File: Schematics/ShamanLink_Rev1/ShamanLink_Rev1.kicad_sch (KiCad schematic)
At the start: 37 parts, among them J6 USB4105-GF-A, U1 LPC55S69JBD64K

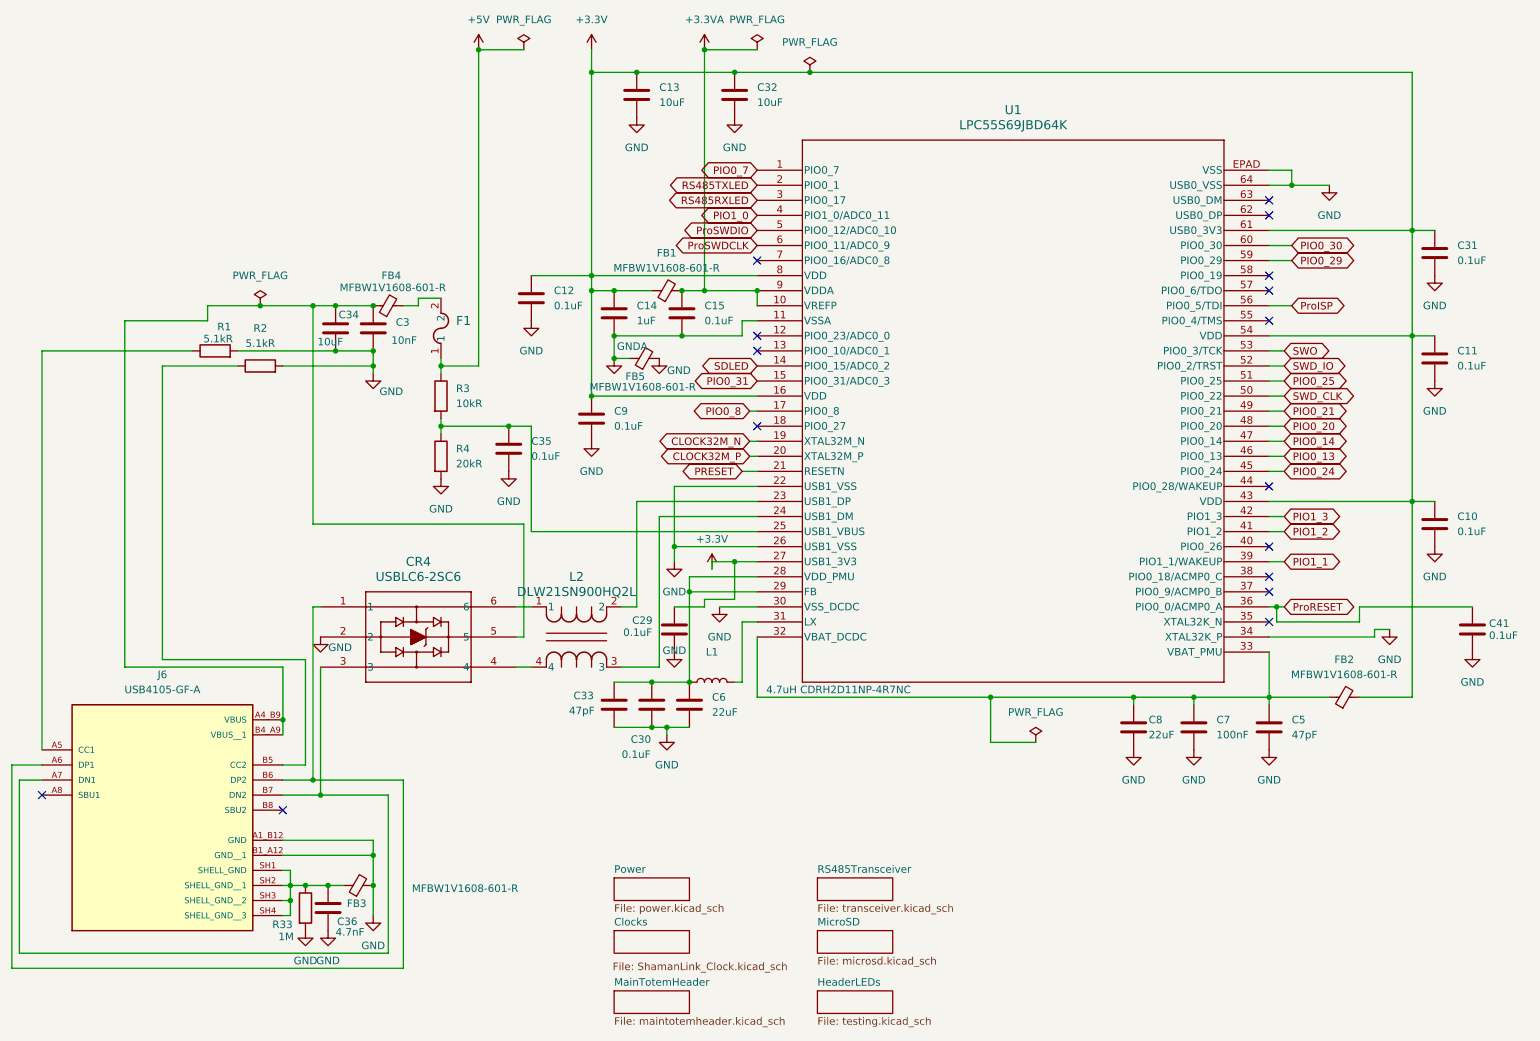
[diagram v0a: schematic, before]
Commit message: Final ShamanLink Revisions and Motor Totem Final Revisions
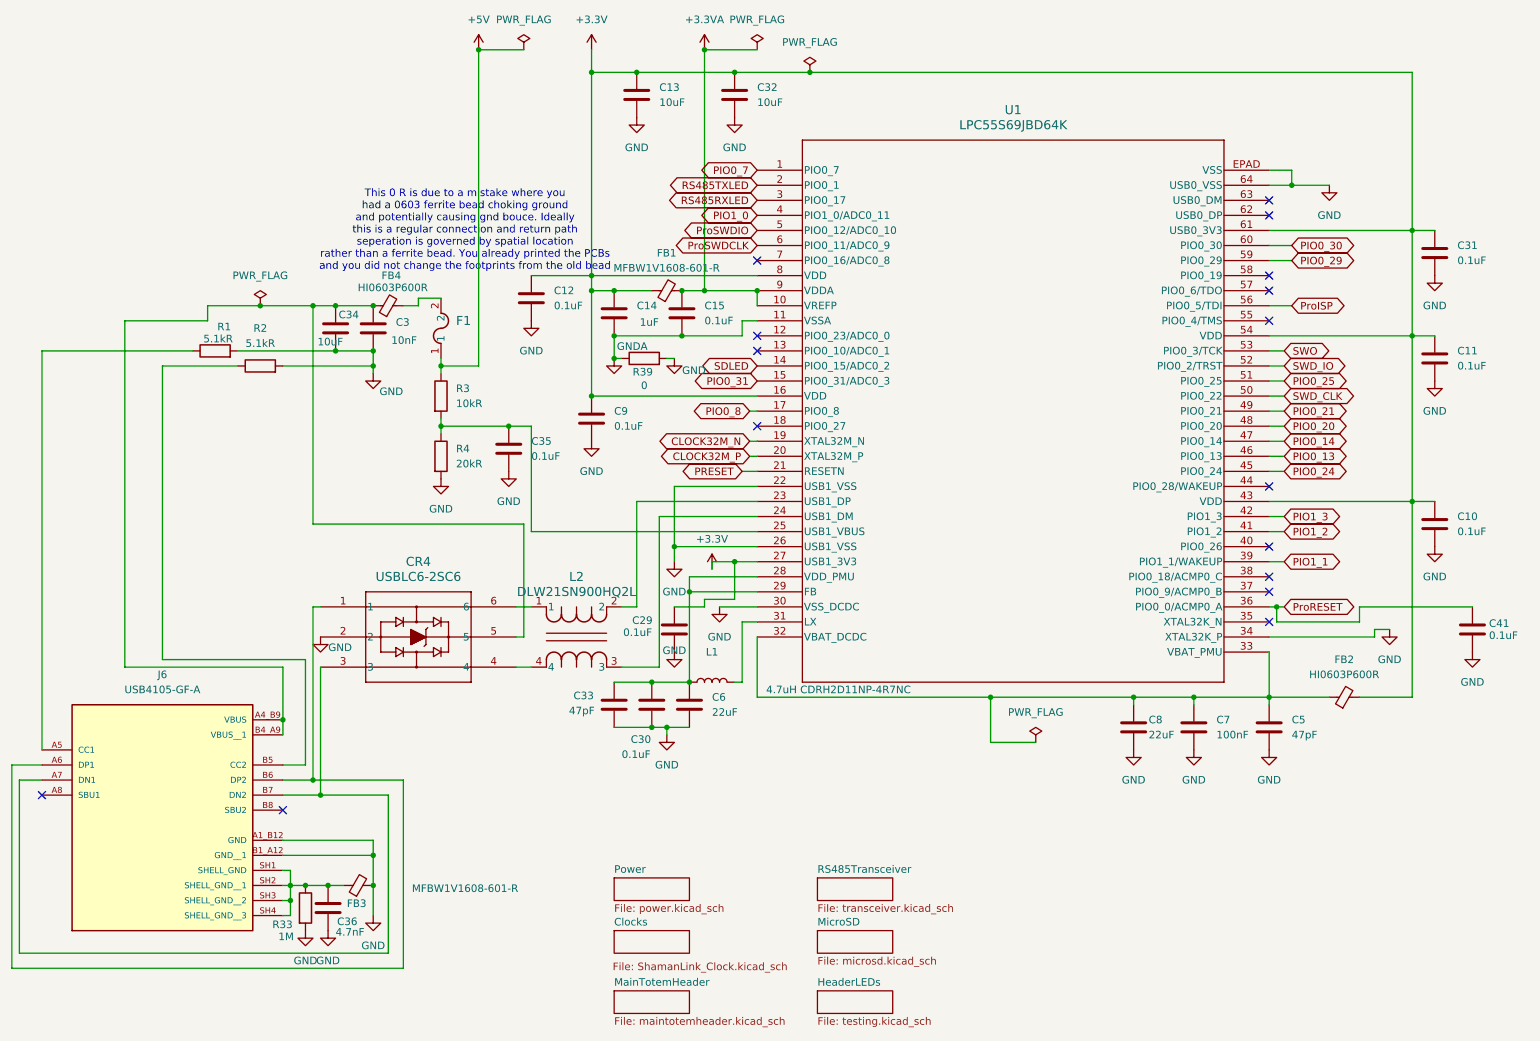
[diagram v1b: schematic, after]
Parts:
- removed FB5: MFBW1V1608-601-R, Resistor_SMD:R_0603_1608Metric_Pad0.98x0.95mm_HandSolder, symbol Device:FerriteBead_Small
- added R39: 0, symbol Device:R
- FB2, FB4: value MFBW1V1608-601-R -> HI0603P600R
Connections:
- net GND: now also R39.2
- net GNDA: now also R39.1
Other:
- note added: "This 0 R is due to a mistake where you had a 0603 ferrite bead choking ground and potentially causing gnd bouce. Ideally this is a regular connection and return path seperation is governed by spatial location rather than a ferrite bead. You already printed the PCBs and you did not change the footprints from the old bead"
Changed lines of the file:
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@@
 		(title "MCU and USB")
 	)
+	(text "This 0 R is due to a mistake where you \nhad a 0603 ferrite bead choking ground\nand potentially causing gnd bouce. Ideally\nthis is a regular connection and return path \nseperation is governed by spatial location \nrather than a ferrite bead. You already printed the PCBs\nand you did not change the footprints from the old bead"
+		(exclude_from_sim no)
+		(at 90.424 63.5 0)
+		(effects
+			(font
+				(size 1.27 1.27)
+			)
+		)
+	)
 	(junction
 		(at 115.57 73.66)
@@
 	)
 	(junction
-		(at 68.58 83.82)
+		(at 115.57 85.09)
 		(diameter 0)
 		(color 0 0 0 0)
 	)
 	(junction
-		(at 60.96 176.53)
+		(at 68.58 83.82)
 		(diameter 0)
 		(color 0 0 0 0)
 	)
 	(junction
-		(at 111.76 71.12)
+		(at 60.96 176.53)
 		(diameter 0)
 		(color 0 0 0 0)
 	)
 	(junction
-		(at 115.57 85.09)
+		(at 111.76 71.12)
 		(diameter 0)
 		(color 0 0 0 0)
@@
 	(wire
 		(pts
+			(xy 115.57 85.09) (xy 116.84 85.09)
+		)
+		(stroke
+			(width 0)
+			(type default)
+		)
+	)
+	(wire
+		(pts
 			(xy 63.5 135.89) (xy 63.5 153.67)
 		)
@@
 	(wire
 		(pts
+			(xy 124.46 85.09) (xy 125.73 85.09)
+		)
+		(stroke
+			(width 0)
+			(type default)
+		)
+	)
+	(wire
+		(pts
 			(xy 86.36 86.36) (xy 86.36 87.63)
 		)
@@
 	(wire
 		(pts
-			(xy 115.57 85.09) (xy 118.11 85.09)
-		)
-		(stroke
-			(width 0)
-			(type default)
-		)
-	)
-	(wire
-		(pts
 			(xy 74.93 173.99) (xy 74.93 179.07)
 		)
@@
 			)
 		)
-		(property "Value" "MFBW1V1608-601-R"
+		(property "Value" "HI0603P600R"
 			(at 78.232 73.152 90)
 			(effects
@@
 			)
 		)
-		(property "Value" "MFBW1V1608-601-R"
+		(property "Value" "HI0603P600R"
 			(at 238.7219 138.43 90)
 			(effects
@@
 		(on_board yes)
 		(dnp no)
-		(fields_autoplaced yes)
 		(property "Reference" "C14"
 			(at 119.38 76.1999 0)
@@
 		)
 		(property "Value" "1uF"
-			(at 119.38 78.7399 0)
+			(at 119.888 78.994 0)
 			(effects
 				(font
@@
 	(symbol
 		(lib_id "power:GND")
-		(at 123.19 85.09 0)
+		(at 125.73 85.09 0)
 		(unit 1)
 		(exclude_from_sim no)
@@
 		(dnp no)
 		(property "Reference" "#PWR022"
-			(at 123.19 91.44 0)
+			(at 125.73 91.44 0)
 			(effects
 				(font
@@
 		)
 		(property "Value" "GND"
-			(at 126.492 87.122 0)
+			(at 129.032 87.122 0)
 			(effects
 				(font
@@
 		)
 		(property "Footprint" ""
-			(at 123.19 85.09 0)
+			(at 125.73 85.09 0)
 			(effects
 				(font
@@
 		)
 		(property "Datasheet" ""
-			(at 123.19 85.09 0)
+			(at 125.73 85.09 0)
 			(effects
 				(font
@@
 		)
 		(property "Description" "Power symbol creates a global label with name \"GND\" , ground"
-			(at 123.19 85.09 0)
+			(at 125.73 85.09 0)
 			(effects
 				(font
@@
 	)
 	(symbol
+		(lib_id "Device:R")
+		(at 120.65 85.09 90)
+		(unit 1)
+		(exclude_from_sim no)
+		(in_bom yes)
+		(on_board yes)
+		(dnp no)
+		(property "Reference" "R39"
+			(at 120.396 87.376 90)
+			(effects
+				(font
+					(size 1.27 1.27)
+				)
+			)
+		)
+		(property "Value" "0"
+			(at 120.65 89.662 90)
+			(effects
+				(font
+					(size 1.27 1.27)
+				)
+			)
+		)
+		(property "Footprint" ""
+			(at 120.65 86.868 90)
+			(effects
+				(font
+					(size 1.27 1.27)
+				)
+				(hide yes)
+			)
+		)
+		(property "Datasheet" "~"
+			(at 120.65 85.09 0)
+			(effects
+				(font
+					(size 1.27 1.27)
+				)
+				(hide yes)
+			)
+		)
+		(property "Description" "Resistor"
+			(at 120.65 85.09 0)
+			(effects
+				(font
+					(size 1.27 1.27)
+				)
+				(hide yes)
+			)
+		)
+		(pin "2"
+		)
+		(pin "1"
+		)
+		(instances
+			(project ""
+				(path "/04556d6e-fcef-428e-bd2f-e6a401b90373"
+					(reference "R39")
+					(unit 1)
+				)
+			)
+		)
+	)
+	(symbol
 		(lib_id "power:PWR_FLAG")
 		(at 55.88 76.2 0)
@@
 					(unit 1)
 				)
-			)
-		)
-	)
-	(symbol
-		(lib_id "Device:FerriteBead_Small")
-		(at 120.65 85.09 90)
-		(unit 1)
-		(exclude_from_sim no)
-		(in_bom yes)
-		(on_board yes)
-		(dnp no)
-		(property "Reference" "FB5"
-			(at 119.126 88.138 90)
-			(effects
-				(font
-					(size 1.27 1.27)
-				)
-			)
-		)
-		(property "Value" "MFBW1V1608-601-R"
-			(at 120.396 89.916 90)
-			(effects
-				(font
-					(size 1.27 1.27)
-				)
-			)
-		)
-		(property "Footprint" "Resistor_SMD:R_0603_1608Metric_Pad0.98x0.95mm_HandSolder"
-			(at 120.65 86.868 90)
-			(effects
-				(font
-					(size 1.27 1.27)
-				)
-				(hide yes)
-			)
-		)
-		(property "Datasheet" "~"
-			(at 120.65 85.09 0)
-			(effects
-				(font
-					(size 1.27 1.27)
-				)
-				(hide yes)
-			)
-		)
-		(property "Description" "Ferrite bead, small symbol"
-			(at 120.65 85.09 0)
-			(effects
-				(font
-					(size 1.27 1.27)
-				)
-				(hide yes)
-			)
-		)
-		(pin "1"
-		)
-		(pin "2"
-		)
-		(instances
-			(project "ShamanLink_Rev1"
-				(path "/04556d6e-fcef-428e-bd2f-e6a401b90373"
-					(reference "FB5")
-					(unit 1)
-				)
